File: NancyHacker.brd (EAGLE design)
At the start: 15.2 x 20.3 mm, 7 parts, among them U1 LM3480IM4, U2 ATTINY24QFN

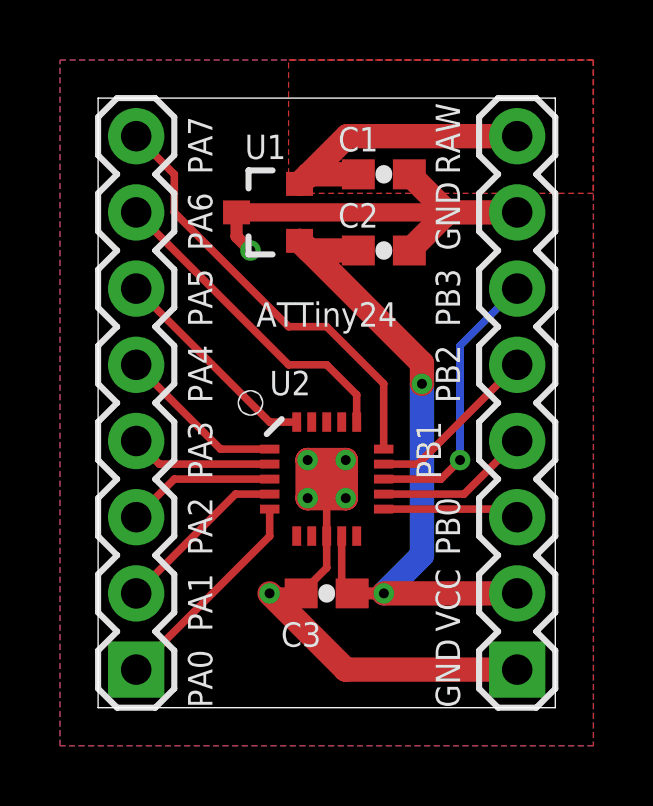
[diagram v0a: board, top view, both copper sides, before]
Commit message: Initial commit of forked NancyHacker (Prototype 1)
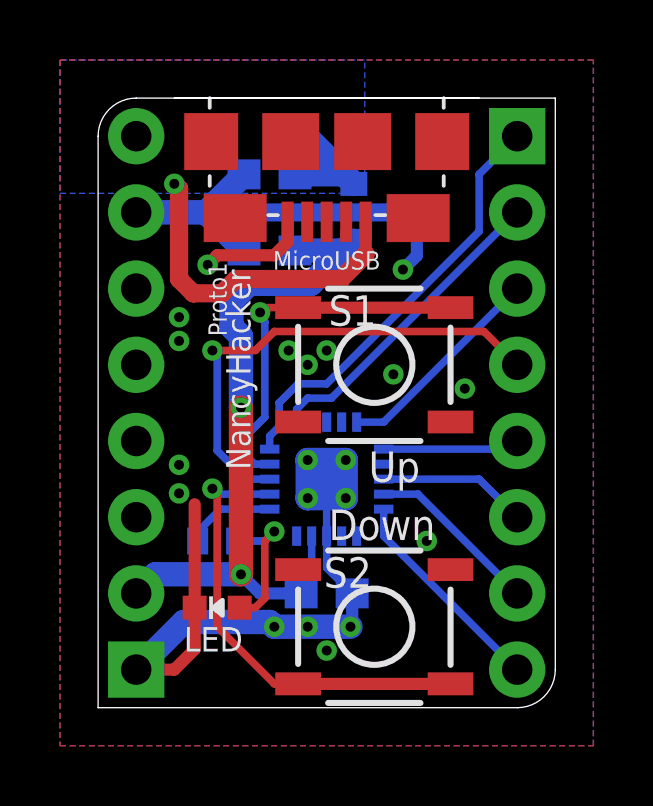
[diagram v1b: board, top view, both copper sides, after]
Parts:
- added LED: 20mA, microbuilder:CHIPLED_0603_NOOUTLINE
- added R2: 200 Ohm, SparkFun-Resistors:0402-RES
- added S1: Up, SparkFun-Electromechanical:TACTILE_SWITCH_SMD
- added S2: Down, SparkFun-Electromechanical:TACTILE_SWITCH_SMD
- added U$1: USB-MICROB-SMDRECEPT, logxen:USB-MICROB-RECEPT
- moved JP1 21.8 mm to (14.0, 19.1), flipped to the bottom, turned to 270 degrees
- moved JP2 12.7 mm to (1.27, 1.27), flipped to the bottom
- moved C1 3.81 mm to (5.71, 17.8), flipped to the bottom
- moved C2 3.81 mm to (5.71, 15.2), flipped to the bottom
- moved U1 3.81 mm to (9.53, 16.5), flipped to the bottom
- flipped C3 to the bottom
- flipped U2 to the bottom
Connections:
- removed net PB0: JP2.3, U2.11
- removed net PB1: JP2.4, U2.12
- removed net PB2: JP2.5, U2.14
- removed net RAW: C1.1, JP2.8, U1.2
- new net 5V: C1.1, U$1.1, U1.2
- new net DOWN: S2.1, S2.2, U2.12
- new net LED: R2.1, U2.11
- new net STATUS_LED_RESISTOR: LED.A, R2.2
- new net UP: S1.1, S1.2, U2.14
- net GND: now also LED.C, S1.3, S1.4, S2.3, S2.4, U$1.5
- net PA0: now also JP1.8; no longer JP1.1
- net PA1: now also JP1.7; no longer JP1.2
- net PA2: now also JP1.6; no longer JP1.3
- net PA3: no longer JP1.4
- net PA5: now also JP1.3; no longer JP1.6
- net PA6: now also JP1.2; no longer JP1.7
- net PA7: now also JP1.1; no longer JP1.8
- net PB3: now also JP1.4; no longer JP2.6
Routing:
- net 5V: track 0.00 -> 15.6 mm, vias 0 -> 1
- net DOWN: track 0.00 -> 15.2 mm, vias 0 -> 1
- net UP: track 0.00 -> 12.4 mm, vias 0 -> 1
- net RAW: track 10.0 -> 0.00 mm
- net GND: track 37.5 -> 47.5 mm, vias 6 -> 20
- net PB3: track 9.31 -> 16.4 mm
- net PB2: track 5.82 -> 0.00 mm
- net PB1: track 5.18 -> 0.00 mm
- net PA3: track 4.77 -> 0.00 mm
- net STATUS_LED_RESISTOR: track 0.00 -> 4.71 mm, vias 0 -> 1
- net PB0: track 4.56 -> 0.00 mm
- net LED: track 0.00 -> 3.02 mm
- net PA4: track 5.61 -> 4.56 mm
- net VCC: track 23.6 -> 24.3 mm
- added copper zone on layer 16, net 5V
- removed copper zone on layer 1, net RAW
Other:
- outline, holes or cut-outs redrawn
- board text added: "!EN!"
- board text added: "!PRG!"
- board text added: "!RST!"
- board text added: "!SLP!"
- board text added: "DIR"
- board text added: "MS1"
- board text added: "MS2"
- board text added: "MicroUSB"
- board text added: "NancyHacker"
- board text added: "Proto1"
- board text added: "STEP"
- board text added: "VDD"
- board text removed: "ATTiny24"
- board text removed: "MISO"
- board text removed: "MOSI"
- board text removed: "PA0"
- board text removed: "PA1"
- board text removed: "PA2"
- board text removed: "PA3"
- board text removed: "PA4"
- board text removed: "PA5"
- board text removed: "PA6"
- board text removed: "PA7"
- board text removed: "PB0"
- board text removed: "PB1"
- board text removed: "PB2"
- board text removed: "PB3"
- board text removed: "RAW"
- board text removed: "RST"
- board text removed: "SCL"
- board text removed: "VCC"
